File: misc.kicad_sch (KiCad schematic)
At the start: 62 parts, among them J1 Serial 1, J10 SW2, J11 SW2, J12 SW2, J13 Rotary Encoder, J14 Paddles, J15 Conn_02x07_Row_Letter_Last, J17 Conn_02x04_Row_Letter_Last, J18 Conn_02x04_Top_Bottom, J19 I2C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

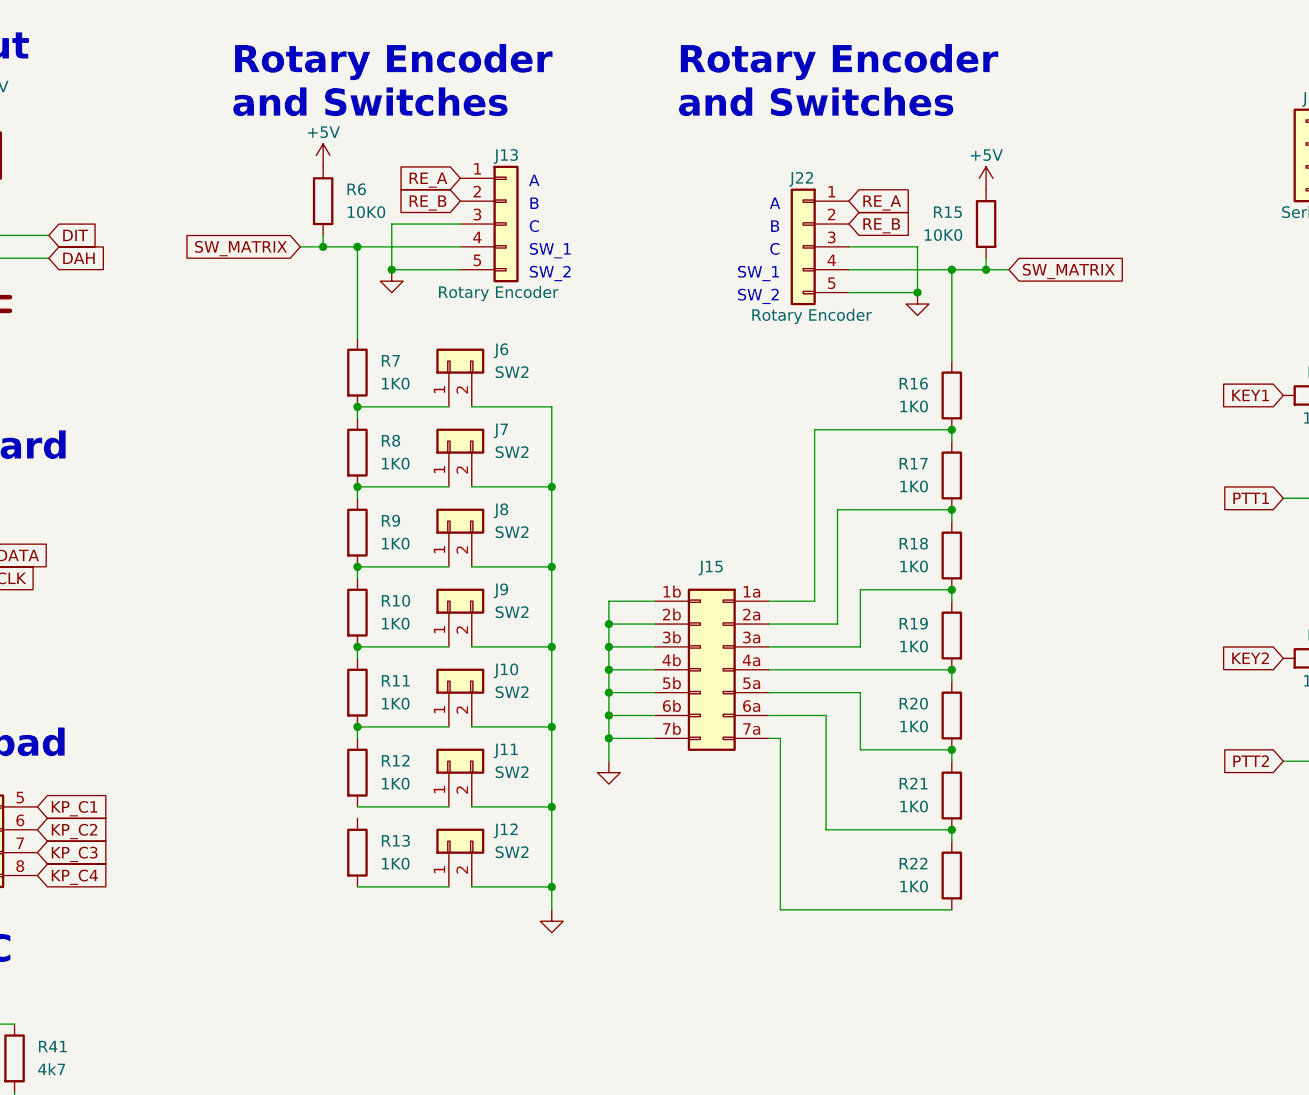
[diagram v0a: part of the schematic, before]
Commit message: Removed version of Rotary Encoder and Switches that didn't use 2x8 pin connector.
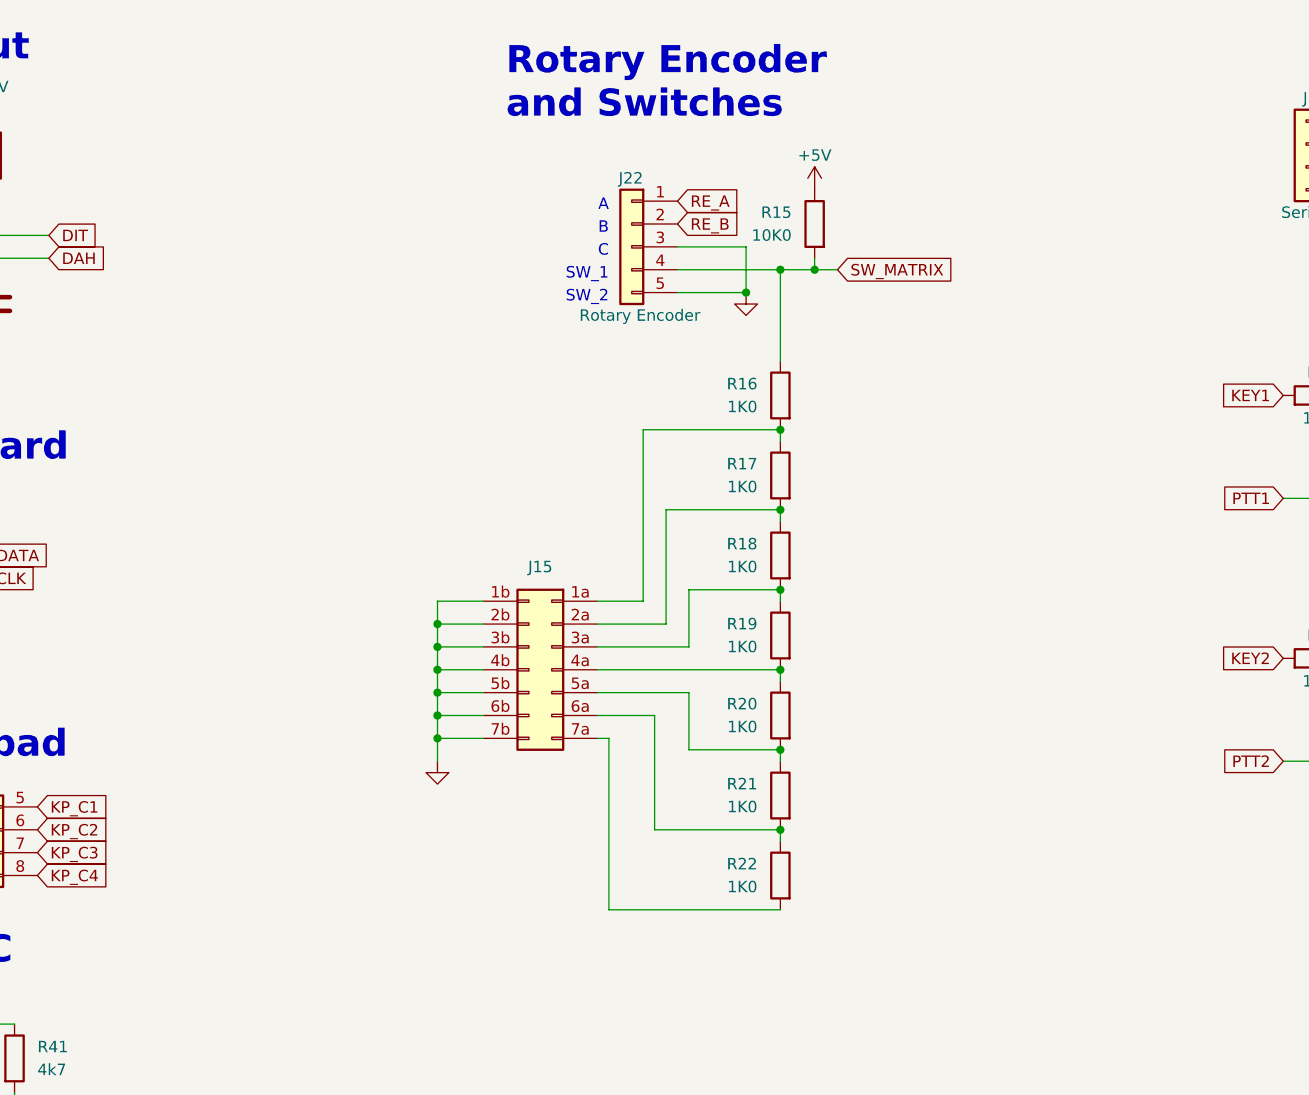
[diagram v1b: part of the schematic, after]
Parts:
- removed J10, J11, J12, J6, J7, J8, J9: SW2, symbol Connector_Generic:Conn_01x02
- removed J13: Rotary Encoder, symbol Connector_Generic:Conn_01x05
- removed R10, R11, R12, R13, R7, R8, R9: 1K0, symbol Device:R
- removed R6: 10K0, symbol Device:R
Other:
- moved on the sheet: J15, J22, R15, R16, R17, R18, R19, R20, R21, R22

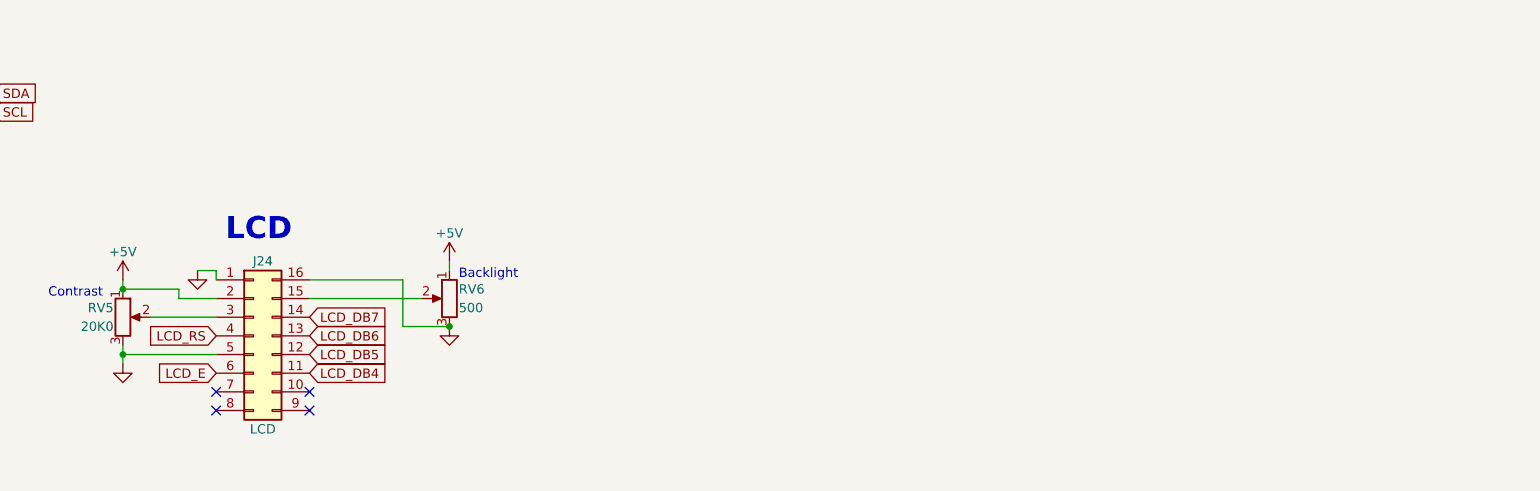
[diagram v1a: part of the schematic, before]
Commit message: Minor changes. Added mounting holes.
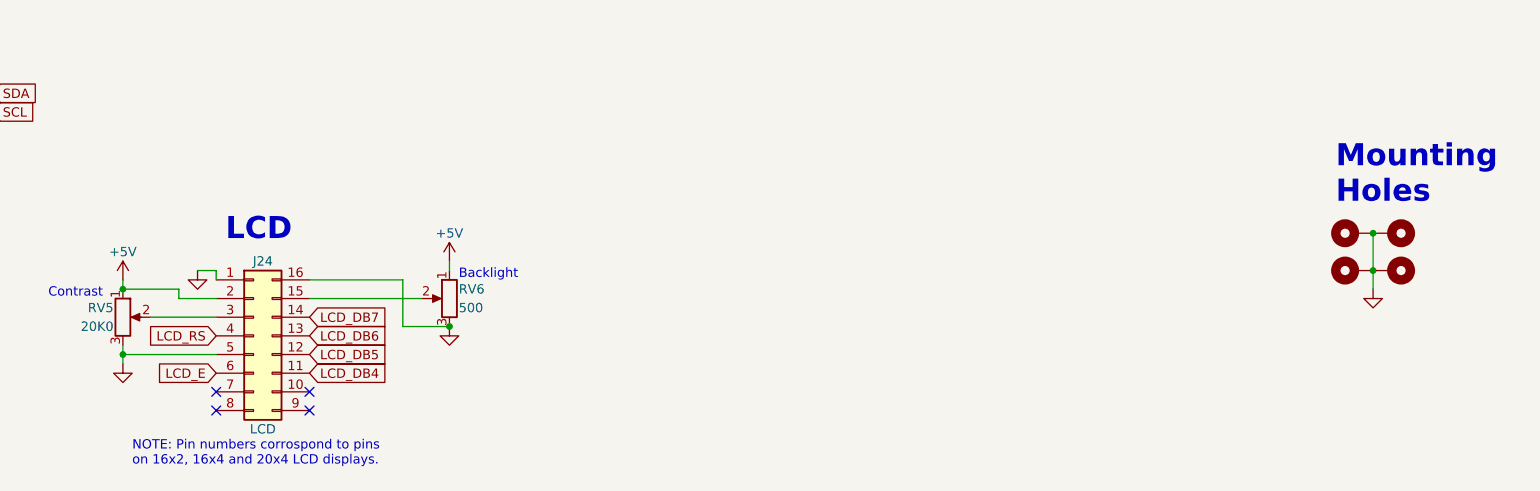
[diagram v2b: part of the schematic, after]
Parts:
- added H1, H2, H3, H4: MountingHole_Pad, symbol Mechanical:MountingHole_Pad
- C1, C2, C3, C4, C5, C6: footprint (none) -> Capacitor_SMD:C_1206_3216Metric; JLCPCB_PN (none) -> C2915712
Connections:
- net GND: now also H1.1, H2.1, H3.1, H4.1
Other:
- note added: "Mounting Holes"
- note added: "NOTE: Pin numbers corrospond to pins on 16x2, 16x4 and 20x4 LCD displays."

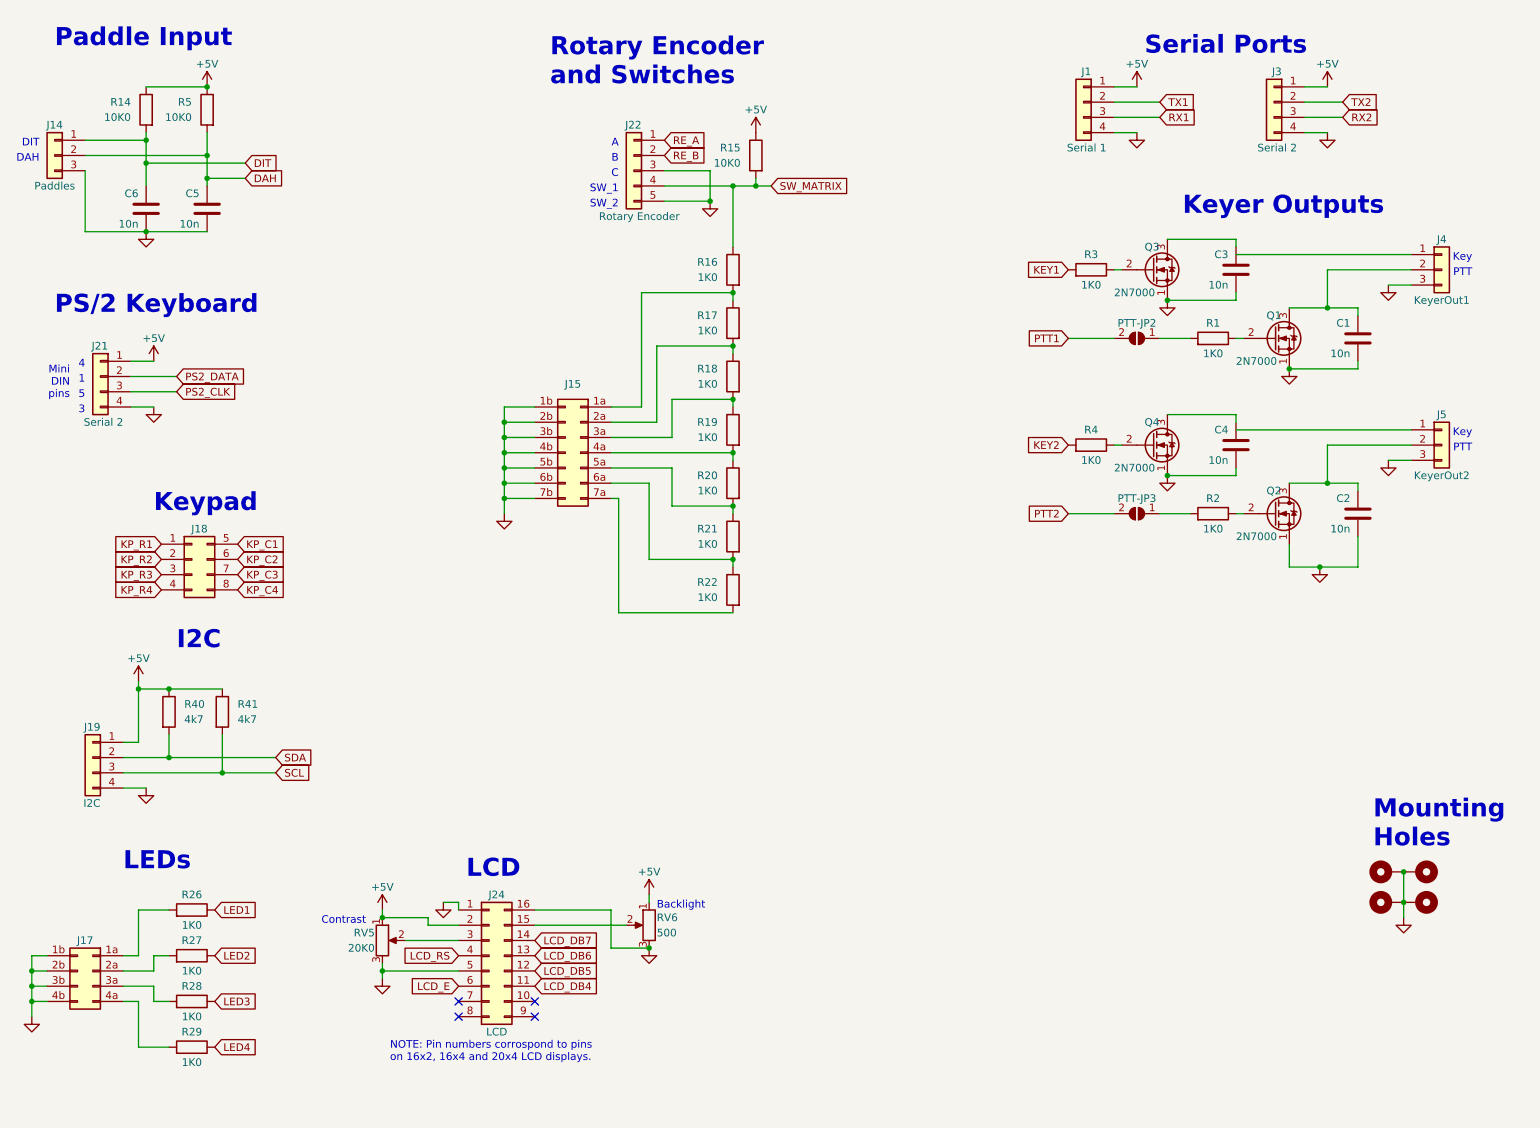
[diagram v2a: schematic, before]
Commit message: Added multi-hole strips to unused pins on Arduino Mega 2560 microprocessor. Also, some minor changes.
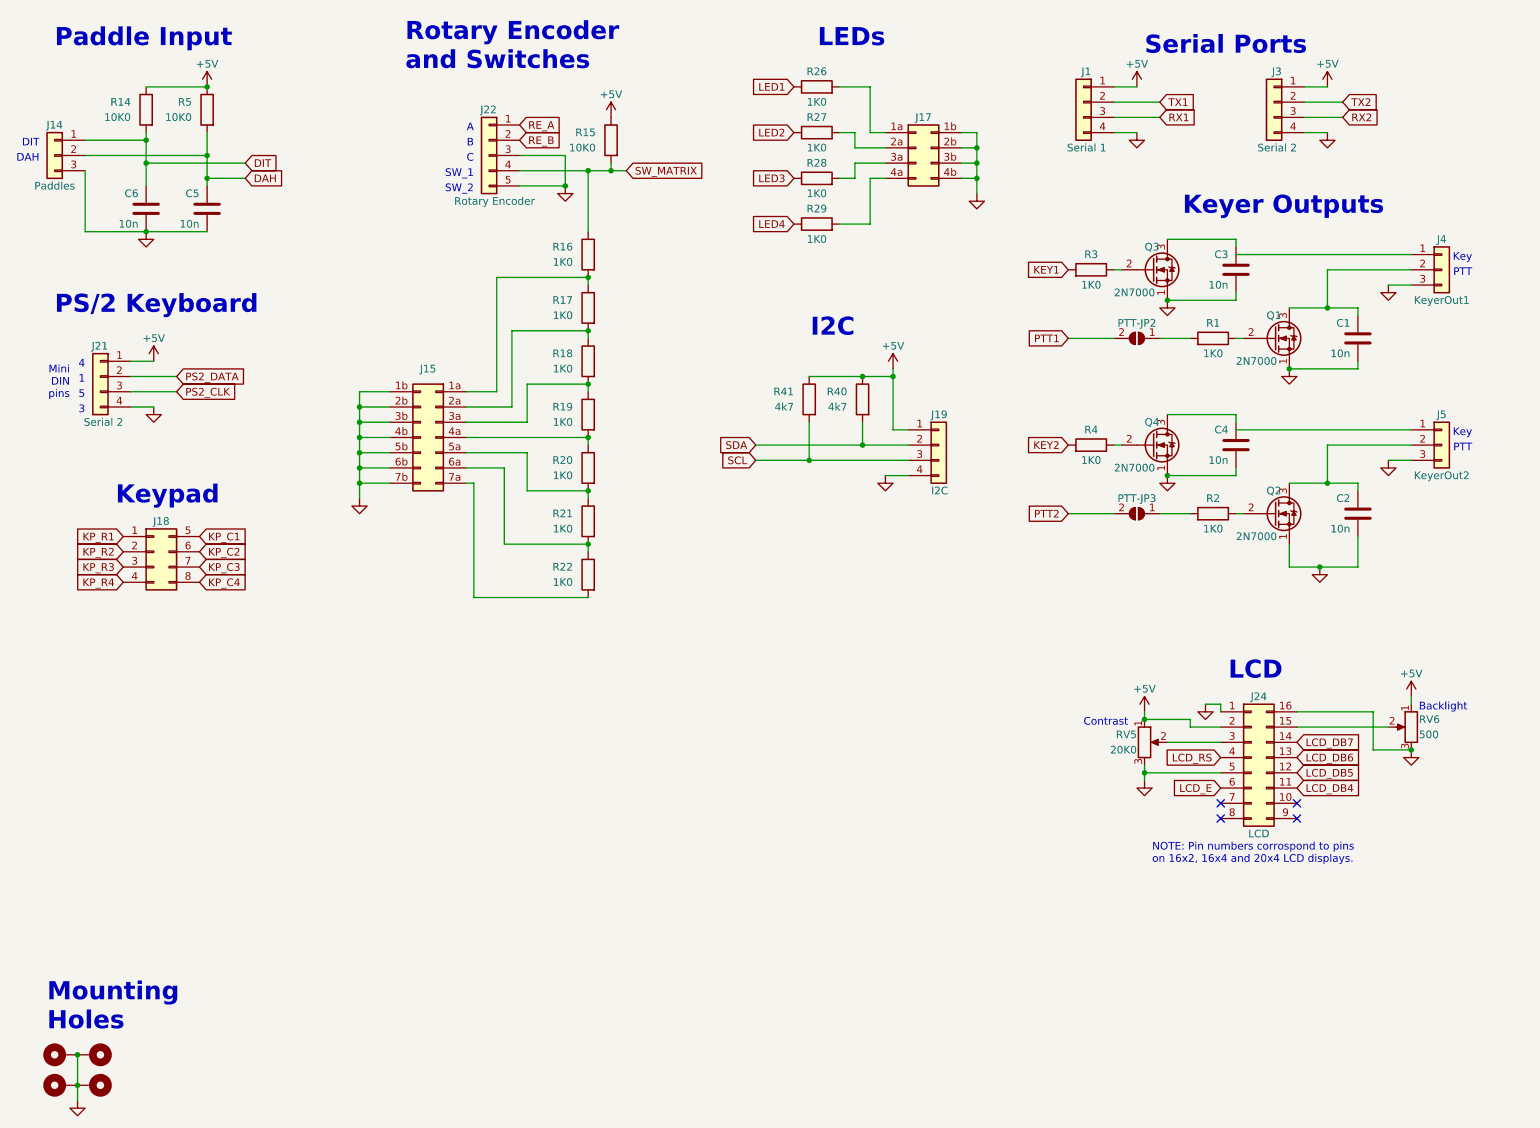
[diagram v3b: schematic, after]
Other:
- moved on the sheet: J15, J17, J18, J19, J22, J24, R15, R16, R17, R18, R19, R20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

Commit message: First attempt at assigning footprints and JLCPCB part numbers.
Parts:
- C1, C2, C3, C4, C5, C6: JLCPCB_PN C2915712 -> C2169061
- H1, H2, H3, H4: footprint (none) -> MountingHole:MountingHole_4.3mm_M4_Pad
- J1, J21, J3: footprint (none) -> Connector_PinHeader_2.54mm:PinHeader_1x04_P2.54mm_Vertical; JLCPCB_PN (none) -> DNP
- J14, J4, J5: footprint (none) -> Connector_PinHeader_2.54mm:PinHeader_1x03_P2.54mm_Vertical; JLCPCB_PN (none) -> DNP
- J15: footprint (none) -> Connector_PinHeader_2.54mm:PinHeader_2x07_P2.54mm_Vertical; JLCPCB_PN (none) -> DNP
- J17, J18, J19: footprint (none) -> Connector_PinHeader_2.54mm:PinHeader_2x04_P2.54mm_Vertical; JLCPCB_PN (none) -> DNP
- J22, PTT-JP2, PTT-JP3: footprint (none) -> Connector_PinHeader_2.54mm:PinHeader_1x05_P2.54mm_Vertical; JLCPCB_PN (none) -> DNP
- J24: footprint (none) -> Connector_PinHeader_2.54mm:PinHeader_2x08_P2.54mm_Vertical; JLCPCB_PN (none) -> DNP
- Q1, Q2, Q3, Q4: footprint Package_TO_SOT_THT:TO-92_Inline -> Package_TO_SOT_SMD:SOT-23; JLCPCB_PN (none) -> C414015
- R1, R16, R17, R18, R19, R2, R20, R21, R22, R26, R27, R28, R29, R3, R4: value 1K0 -> 1k; footprint (none) -> Resistor_SMD:R_0805_2012Metric; JLCPCB_PN (none) -> C4033501
- R14, R15, R5: value 10K0 -> 10k; footprint (none) -> Resistor_SMD:R_0805_2012Metric; JLCPCB_PN (none) -> C17414
- R40, R41: footprint (none) -> Resistor_SMD:R_0805_2012Metric; JLCPCB_PN (none) -> C17673
- RV5: value 20K0 -> 20k; footprint (none) -> Resistor_SMD:R_0805_2012Metric; JLCPCB_PN (none) -> C4340265
- RV6: value 500 -> 500R; footprint (none) -> Resistor_SMD:R_0805_2012Metric; JLCPCB_PN (none) -> C2828857

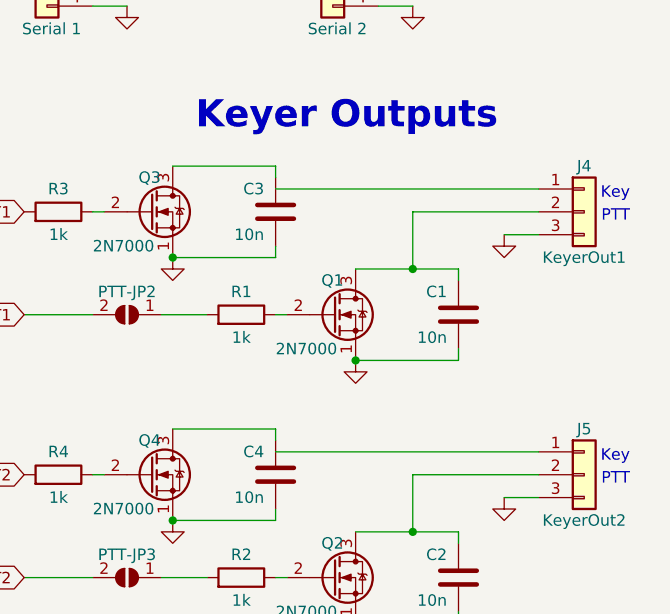
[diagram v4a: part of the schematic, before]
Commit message: Added PWR_FLAG and others to correct ERC errors. All ERC errors corrected; no errors or warnings present.
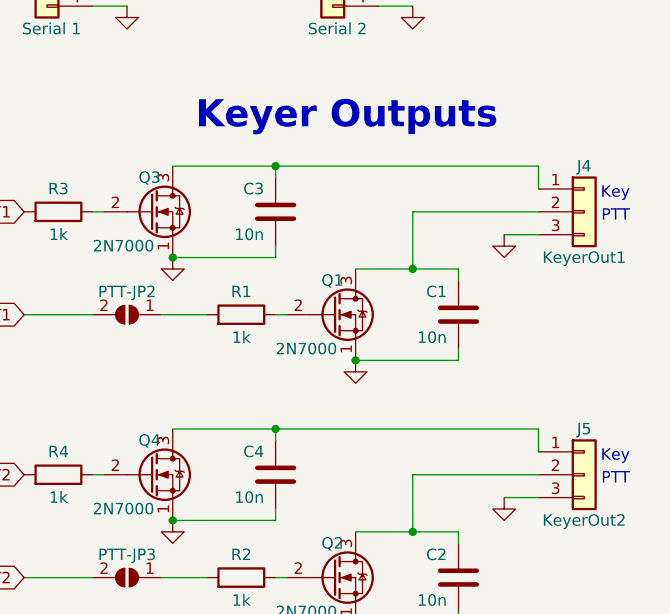
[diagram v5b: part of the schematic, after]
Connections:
- net at C3.1, Q3.3 (D): now also J4.1 (Pin_1)
- net at C4.1, Q4.3 (D): now also J5.1 (Pin_1)
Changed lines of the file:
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@@
   (junction (at 36.83 50.8) (diameter 0) (color 0 0 0 0)
   )
+  (junction (at 218.44 52.07) (diameter 0) (color 0 0 0 0)
+  )
   (junction (at 72.39 85.09) (diameter 0) (color 0 0 0 0)
   )
@@
   )
   (junction (at 110.49 85.09) (diameter 0) (color 0 0 0 0)
+  )
+  (junction (at 218.44 81.28) (diameter 0) (color 0 0 0 0)
   )
   (junction (at 175.26 41.91) (diameter 0) (color 0 0 0 0)
@@
     (stroke (width 0) (type default))
   )
+  (wire (pts (xy 218.44 52.07) (xy 247.65 52.07))
+    (stroke (width 0) (type default))
+  )
   (wire (pts (xy 77.47 85.09) (xy 72.39 85.09))
     (stroke (width 0) (type default))
@@
     (stroke (width 0) (type default))
   )
-  (wire (pts (xy 247.65 83.82) (xy 218.44 83.82))
-    (stroke (width 0) (type default))
-  )
   (wire (pts (xy 152.4 49.53) (xy 157.48 49.53))
     (stroke (width 0) (type default))
@@
     (stroke (width 0) (type default))
   )
+  (wire (pts (xy 247.65 81.28) (xy 247.65 83.82))
+    (stroke (width 0) (type default))
+  )
   (wire (pts (xy 219.71 68.58) (xy 218.44 68.58))
     (stroke (width 0) (type default))
@@
     (stroke (width 0) (type default))
   )
-  (wire (pts (xy 247.65 54.61) (xy 218.44 54.61))
-    (stroke (width 0) (type default))
-  )
   (wire (pts (xy 199.39 86.36) (xy 198.12 86.36))
     (stroke (width 0) (type default))
@@
     (stroke (width 0) (type default))
   )
+  (wire (pts (xy 218.44 81.28) (xy 247.65 81.28))
+    (stroke (width 0) (type default))
+  )
   (wire (pts (xy 97.79 67.31) (xy 97.79 80.01))
     (stroke (width 0) (type default))
@@
     (stroke (width 0) (type default))
   )
+  (wire (pts (xy 247.65 52.07) (xy 247.65 54.61))
+    (stroke (width 0) (type default))
+  )
